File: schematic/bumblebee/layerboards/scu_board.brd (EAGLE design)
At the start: 85 x 100 mm, 13 parts, among them P1 B6B-EH-A, P2 B6B-EH-A, P3 B7B-EH-A, P4 B5B-EH-A, P5 B4B-EH-A, P6 B4B-EH-A, P7 B3B-EH-A

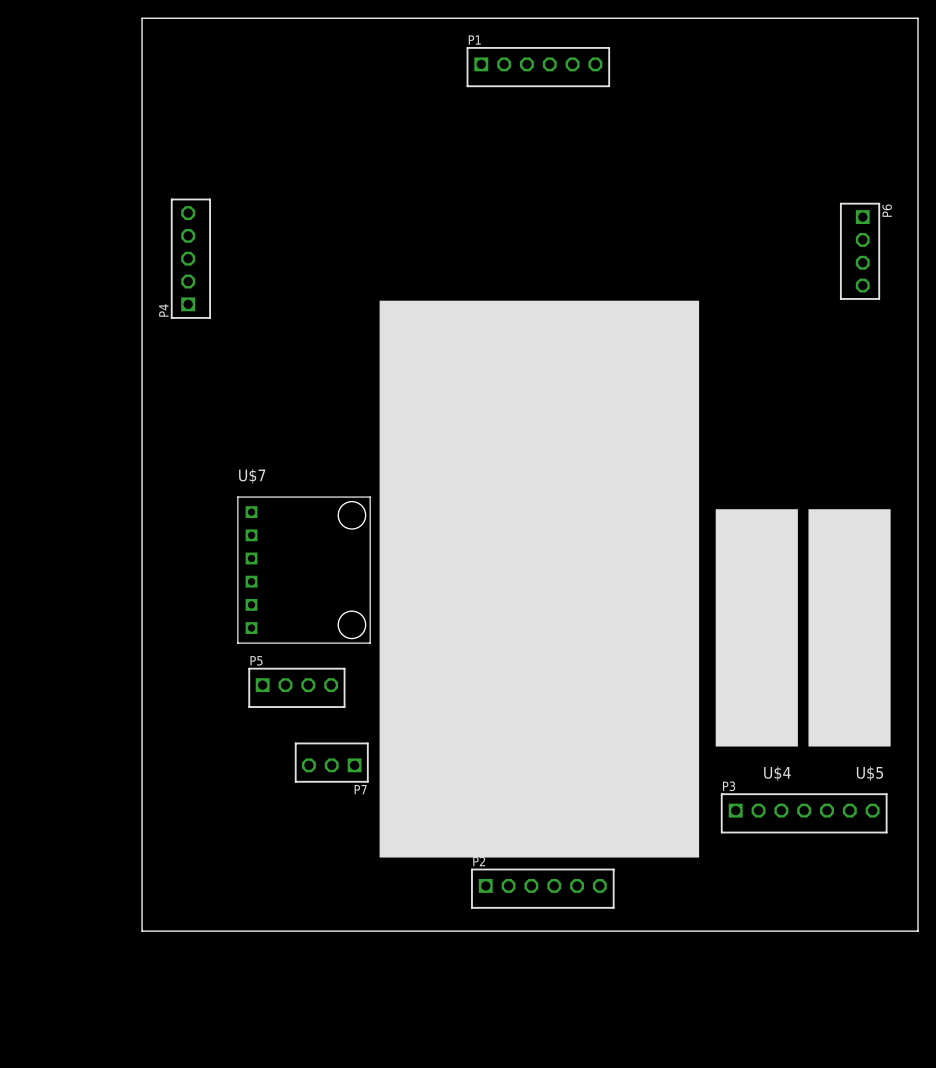
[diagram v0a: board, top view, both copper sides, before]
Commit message: Ведётся работа по платам. Готовы SCU и CCU
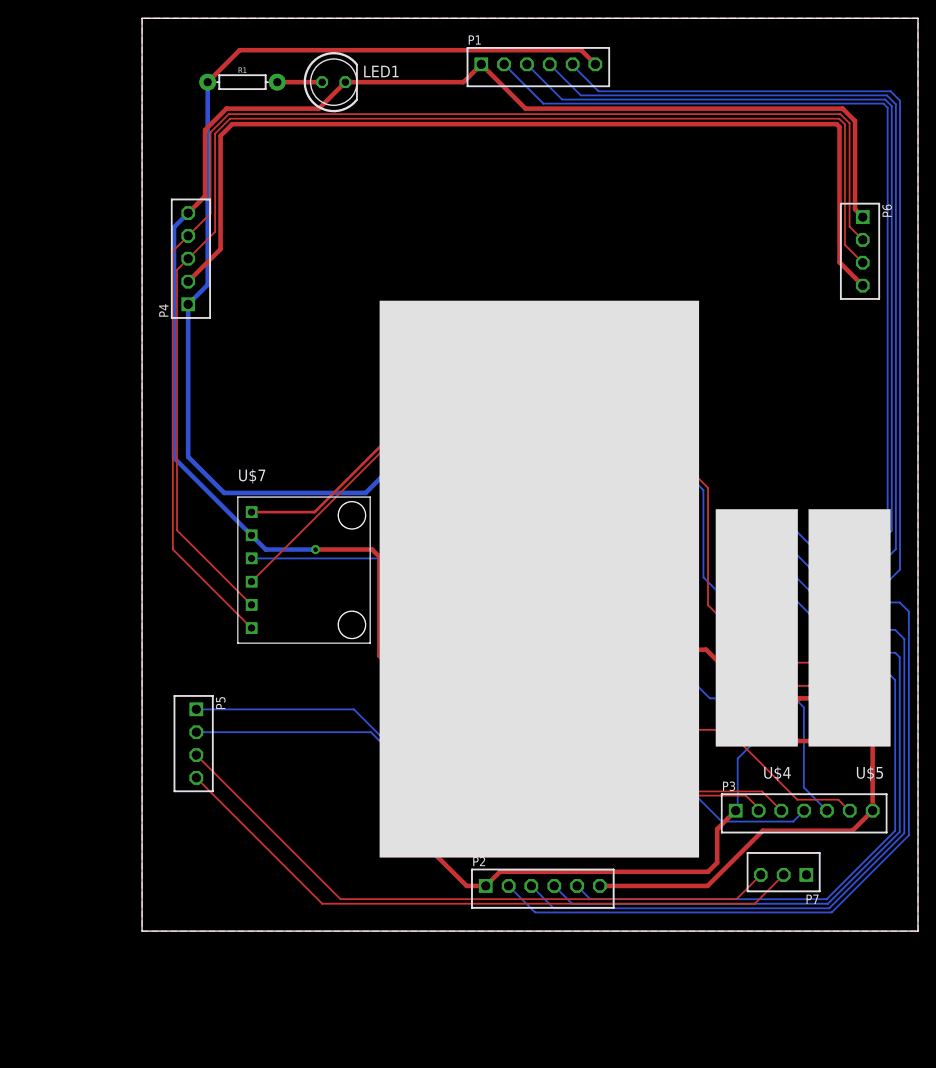
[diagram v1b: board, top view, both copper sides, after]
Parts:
- added LED1: (no value), led:LED5MM
- added R1: 150, SparkFun-Resistors:AXIAL-0.3
- moved P7 50.9 mm to (70.3, 6.16)
- moved P5 12.7 mm to (5.95, 20.5), turned to 270 degrees
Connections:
- new net N$19: LED1.A, R1.P$2
- net 5V_SCU: now also R1.P$1
- net GND: now also LED1.K
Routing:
- net GND: track 0.00 -> 283.1 mm, vias 0 -> 1
- net 5V_SCU: track 0.00 -> 250.2 mm
- net N$25: track 0.00 -> 144.2 mm
- net N$23: track 0.00 -> 142.6 mm
- net 5V_CCU: track 0.00 -> 104.3 mm
- net N$8: track 0.00 -> 92.4 mm
- net N$9: track 0.00 -> 91.4 mm
- net N$10: track 0.00 -> 90.6 mm
- net N$15: track 0.00 -> 90.2 mm
- net N$11: track 0.00 -> 89.8 mm
- net N$14: track 0.00 -> 83.4 mm
- net N$13: track 0.00 -> 77.2 mm
- net N$27: track 0.00 -> 71.4 mm
- net N$12: track 0.00 -> 70.7 mm
- net MAG_CS: track 0.00 -> 69.8 mm
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- added copper zone on layer 1, net GND
- added copper zone on layer 16, net GND

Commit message: CCU и ICU полностью готовы. Было бы здорово, если бы ещё кто-то посмотрел По SCU требуются уточнения
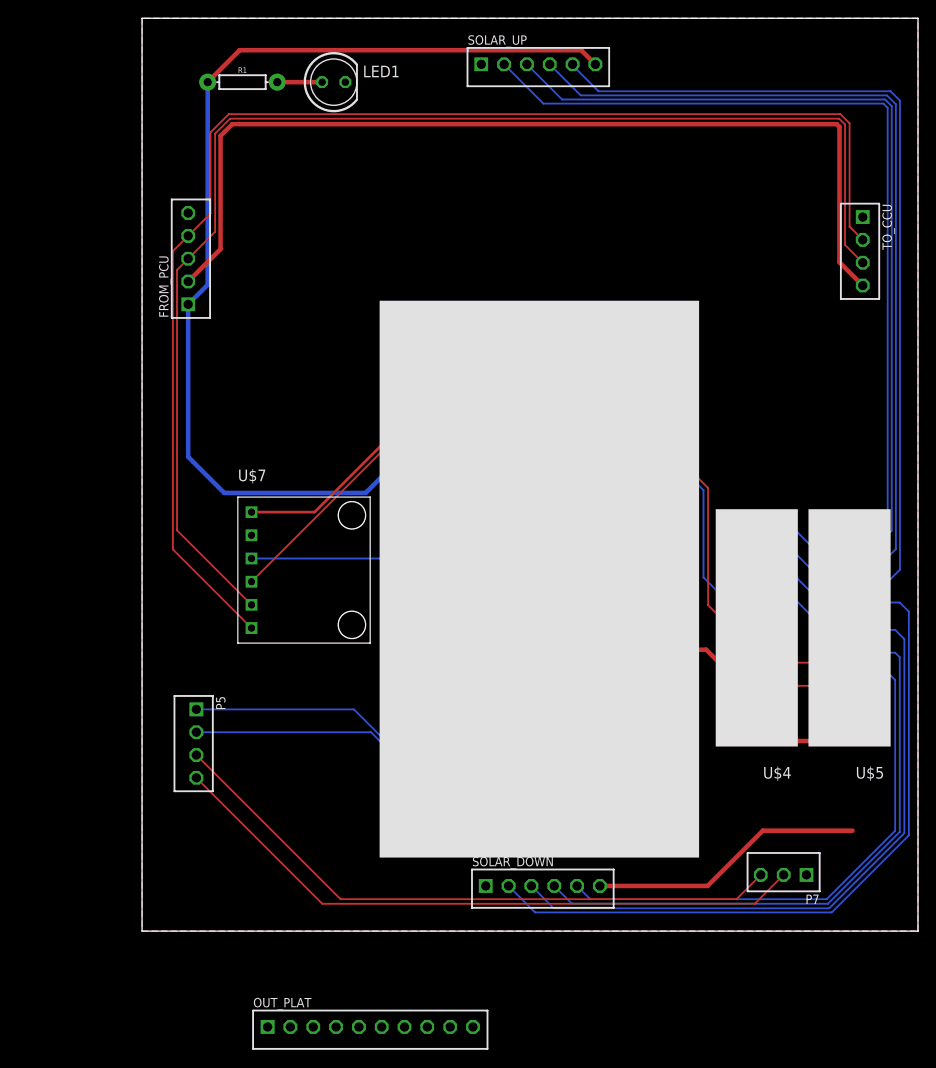
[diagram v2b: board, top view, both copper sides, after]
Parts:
- removed P3: B7B-EH-A, con-jst-eh:B7B-EH-A
- added OUT_PLAT: B10B-EH-A, con-jst-eh:B10B-EH-A
- renumbered P1 to SOLAR_UP, P2 to SOLAR_DOWN, P4 to FROM_PCU, P6 to TO_CCU
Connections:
- net SCL renamed SCL3
- net SDA renamed SDA3
- removed net N$1: U$1.PB8, U$2.SCL
- removed net N$5: U$1.PB9, U$2.SDA
- new net SCL2: OUT_PLAT.9, U$1.PB8, U$2.SCL
- new net SDA2: OUT_PLAT.8, U$1.PB9, U$2.SDA
- net 5V_SCU: now also OUT_PLAT.1; no longer P3.7
- net GND: now also OUT_PLAT.2; no longer P3.1
- net MAG_CLOCK: now also OUT_PLAT.4; no longer P3.3
- net MAG_CS: now also OUT_PLAT.3; no longer P3.2
- net MAG_DATA: now also OUT_PLAT.5; no longer P3.4
- net N$17: now also OUT_PLAT.6; no longer P3.5
- net N$18: now also OUT_PLAT.7; no longer P3.6
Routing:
- net GND: track 283.1 -> 0.00 mm, vias 1 -> 0
- net MAG_CS: track 69.8 -> 0.00 mm
- net MAG_CLOCK: track 62.8 -> 0.00 mm
- net MAG_DATA: track 55.1 -> 0.00 mm
- net N$17: track 29.0 -> 0.00 mm
- net SCL2: track 0.00 -> 26.6 mm
- net N$1: track 26.6 -> 0.00 mm
- net N$18: track 23.2 -> 0.00 mm
- net SDA2: track 0.00 -> 15.5 mm
- net N$5: track 15.5 -> 0.00 mm
- net 5V_SCU: track 250.2 -> 239.4 mm

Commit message: ICU готова, SCU скоро доделаю, пока что там всё не очень В либу добавлен LSM303C
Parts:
- removed U$5: ADS, bluepill:ADS
- added X1, X2, X3, X4, X5: 332-02, con-garry:332-02
- U$4: value ADS -> LSM303C; device bluepill:ADS -> bluepill:LSM303C
- moved U$4 78.2 mm to (-7.00, 9.00), turned to 0 degrees
- moved SOLAR_DOWN 28.6 mm to (16.6, 13.4), turned to 90 degrees
- moved OUT_PLAT 23.0 mm to (41.5, 5.50)
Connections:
- removed net N$10: SOLAR_UP.3, U$5.A2
- removed net N$11: SOLAR_UP.2, U$5.A3
- removed net N$12: SOLAR_DOWN.5, U$4.A0
- removed net N$13: SOLAR_DOWN.4, U$4.A1
- removed net N$14: SOLAR_DOWN.3, U$4.A2
- removed net N$15: SOLAR_DOWN.2, U$4.A3
- removed net N$17: OUT_PLAT.6, U$1.PC1
- removed net N$18: OUT_PLAT.7, U$1.PB1
- removed net N$2: U$1.PA5, U$3.SCL
- removed net N$3: U$1.PA6, U$3.SAD
- removed net N$4: U$1.PA7, U$3.SDA
- removed net N$8: SOLAR_UP.5, U$5.A0
- removed net N$9: SOLAR_UP.4, U$5.A1
- removed net SCL2: OUT_PLAT.9, U$1.PB8, U$2.SCL
- removed net SDA2: OUT_PLAT.8, U$1.PB9, U$2.SDA
- new net 3V3: SOLAR_DOWN.6, SOLAR_UP.6, U$1.3.3V
- new net ADC_OUT_1: OUT_PLAT.7, U$1.PA1
- new net ADC_OUT_2: OUT_PLAT.6, U$1.PA3
- new net MISO_2: U$1.PB14, U$2.SD0
- new net MISO_3: U$1.PC11, U$3.SAD
- new net MOSI_2: U$1.PB15, U$2.SDA
- new net MOSI_3: U$1.PC12, U$3.SDA
- new net NSS_2: U$1.PB12, U$2.CSB
- new net NSS_3: U$1.PD2, U$3.CS
- new net SCK_2: U$1.PB13, U$2.SCL
- new net SCK_3: U$1.PC10, U$3.SCL
- new net SOL_D_1: SOLAR_DOWN.2, U$1.PC2
- new net SOL_D_2: SOLAR_DOWN.3, U$1.PC3
- new net SOL_D_3: SOLAR_DOWN.4, U$1.PC4
- new net SOL_D_4: SOLAR_DOWN.5, U$1.PC5
- new net SOL_U_1: SOLAR_UP.5, U$1.PB1
- new net SOL_U_2: SOLAR_UP.4, U$1.PA7
- new net SOL_U_3: SOLAR_UP.3, U$1.PC1
- new net SOL_U_4: SOLAR_UP.2, U$1.PA5
- net 5V_SCU: now also U$4.5V; no longer SOLAR_DOWN.6, SOLAR_UP.6, U$4.V, U$5.V
- net GND: now also U$4.GND; no longer U$3.CS, U$4.G, U$5.G
- net MAG_CLOCK: now also X4.2; no longer OUT_PLAT.4
- net MAG_CS: now also U$4.CSM, X3.1, X3.2
- net MAG_DATA: now also X5.2; no longer OUT_PLAT.5
- net SCL3: now also OUT_PLAT.9, X1.1, X1.2; no longer U$5.SCL
- net SDA3: now also OUT_PLAT.8, X2.1, X2.2; no longer U$5.SDA
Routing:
- net 3V3: track 0.00 -> 144.7 mm, vias 0 -> 1
- net SOL_U_1: track 0.00 -> 124.7 mm
- net SOL_U_4: track 0.00 -> 124.5 mm
- net SOL_U_3: track 0.00 -> 124.1 mm
- net SOL_U_2: track 0.00 -> 123.8 mm
- net SCL3: track 41.1 -> 147.8 mm
- net MAG_CS: track 0.00 -> 95.1 mm, vias 0 -> 1
- net MAG_CLOCK: track 0.00 -> 94.3 mm, vias 0 -> 1
- net N$8: track 92.4 -> 0.00 mm
- net N$9: track 91.4 -> 0.00 mm
- net N$10: track 90.6 -> 0.00 mm
- net N$15: track 90.2 -> 0.00 mm
- net N$11: track 89.8 -> 0.00 mm
- net 5V_SCU: track 239.4 -> 152.5 mm, vias 0 -> 1
- net N$14: track 83.4 -> 0.00 mm
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
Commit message: Готова SCU и поправил lsm303c в либе
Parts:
- removed OUT_PLAT: B10B-EH-A, con-jst-eh:B10B-EH-A
- removed X1, X2, X3, X4, X5: 332-02, con-garry:332-02
- added P1: B8B-EH-A, con-jst-eh:B8B-EH-A
- moved U$4 85.9 mm to (70.5, 46.0)
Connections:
- removed net MAG_CLOCK: U$3.SCX, X4.2
- removed net MAG_DATA: U$3.SDX, X5.2
- net 5V_SCU: now also P1.1; no longer OUT_PLAT.1
- net ADC_OUT_1: now also P1.5; no longer OUT_PLAT.7
- net ADC_OUT_2: now also P1.4; no longer OUT_PLAT.6
- net GND: now also P1.2; no longer OUT_PLAT.2
- net MAG_CS: now also P1.3; no longer OUT_PLAT.3, X3.1, X3.2
- net SCL3: now also P1.7, U$3.SCX; no longer OUT_PLAT.9, X1.1, X1.2
- net SDA3: now also P1.6, U$3.SDX; no longer OUT_PLAT.8, X2.1, X2.2
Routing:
- net SDA3: track 123.5 -> 223.0 mm, vias 1 -> 2
- net MAG_CLOCK: track 94.3 -> 0.00 mm, vias 1 -> 0
- net SCL3: track 147.8 -> 239.8 mm, vias 0 -> 1
- net MAG_DATA: track 78.5 -> 0.00 mm, vias 1 -> 0
- net 5V_SCU: track 152.5 -> 194.3 mm, vias 1 -> 2
- net MAG_CS: track 95.1 -> 75.3 mm
- net ADC_OUT_1: track 39.0 -> 37.7 mm
- net ADC_OUT_2: track 39.8 -> 38.5 mm
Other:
- board text added: "150"
- board text added: "BME280"
- board text added: "CAN"
- board text added: "DEBUG"
- board text added: "FROM_PCU_BOARD"
- board text added: "LED"
- board text added: "LSM303C"
- board text added: "LSM6DS3"
- board text added: "SOLAR_DOWN"
- board text added: "SOLAR_UP"
- board text added: "TO_CCU_BOARD"
- board text added: "TO_OUT_BOARD"
- board text added: "Спутникостроительный завод 2018-2019"

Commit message: Подготовка плат к производству
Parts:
- removed SOLAR_DOWN, SOLAR_UP: B6B-EH-A, con-jst-eh:B6B-EH-A
- added R2, R3, R4, R5, R6, R7, R8, R9: 150, SparkFun-Resistors:AXIAL-0.3
- added SOL_D_1_2, SOL_D_3_4, SOL_U_1_2, SOL_U_3_4: B4B-EH-A, con-jst-eh:B4B-EH-A
- renumbered P1 to TO_OUT_BOARD, P5 to DEBUG, P7 to DEBUG_OUT
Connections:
- net 3V3: now also SOL_D_1_2.2, SOL_D_1_2.4, SOL_D_3_4.2, SOL_D_3_4.4, SOL_U_1_2.2, SOL_U_1_2.4, SOL_U_3_4.2, SOL_U_3_4.4; no longer SOLAR_DOWN.6, SOLAR_UP.6
- net GND: now also R2.P$1, R3.P$1, R4.P$2, R5.P$1, R6.P$1, R7.P$2, R8.P$2, R9.P$1; no longer SOLAR_DOWN.1, SOLAR_UP.1
- net SOL_D_1: now also R9.P$2, SOL_D_1_2.1; no longer SOLAR_DOWN.2
- net SOL_D_2: now also R8.P$1, SOL_D_1_2.3; no longer SOLAR_DOWN.3
- net SOL_D_3: now also R7.P$1, SOL_D_3_4.1; no longer SOLAR_DOWN.4
- net SOL_D_4: now also R6.P$2, SOL_D_3_4.3; no longer SOLAR_DOWN.5
- net SOL_U_1: now also R5.P$2, SOL_U_1_2.1; no longer SOLAR_UP.5
- net SOL_U_2: now also R4.P$1, SOL_U_1_2.3; no longer SOLAR_UP.4
- net SOL_U_3: now also R3.P$2, SOL_U_3_4.1; no longer SOLAR_UP.3
- net SOL_U_4: now also R2.P$2, SOL_U_3_4.3; no longer SOLAR_UP.2
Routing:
- net SOL_D_1: track 20.6 -> 107.9 mm
- net SOL_D_4: track 28.4 -> 113.4 mm
- net SOL_D_3: track 26.4 -> 109.6 mm
- net SOL_D_2: track 29.7 -> 106.6 mm
- net SOL_U_1: track 124.7 -> 165.2 mm
- net 3V3: track 144.7 -> 183.6 mm
- net SOL_U_2: track 123.8 -> 156.7 mm
- net SOL_U_3: track 124.1 -> 152.0 mm
- net SOL_U_4: track 124.5 -> 144.2 mm
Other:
- board text removed: "150"
- board text removed: "DEBUG"
- board text removed: "FROM_PCU_BOARD"
- board text removed: "LED"
- board text removed: "SOLAR_DOWN"
- board text removed: "SOLAR_UP"
- board text removed: "TO_CCU_BOARD"
- board text removed: "TO_OUT_BOARD"
